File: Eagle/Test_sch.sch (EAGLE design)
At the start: 2 parts, among them U1 APR9600_DIP-28, U2 APR9600_DIP-28

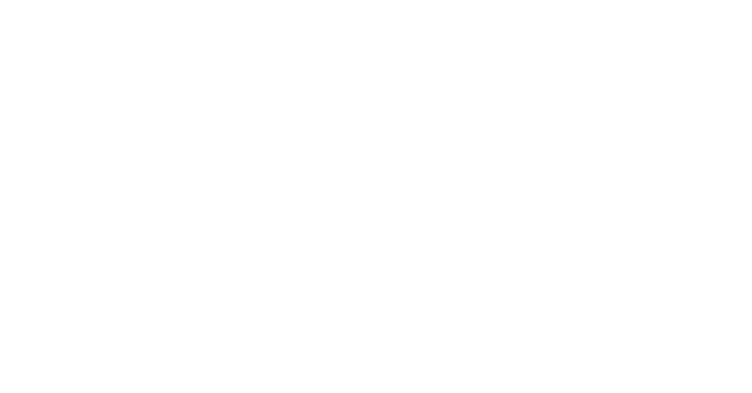
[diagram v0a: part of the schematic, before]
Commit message: La til Buzzer
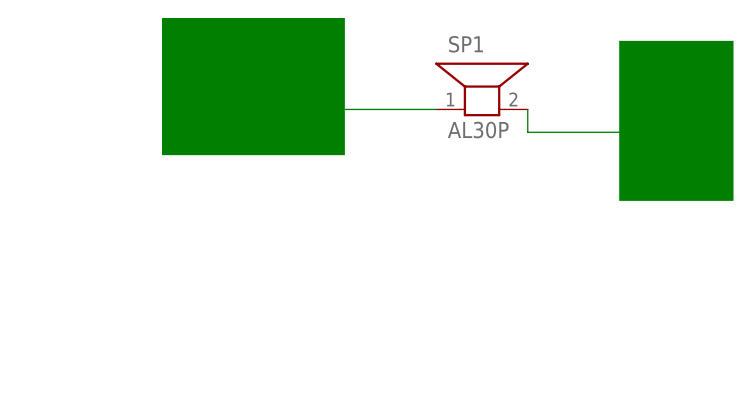
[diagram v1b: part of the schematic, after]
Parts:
- added SP1: AL30P, buzzer:AL30P
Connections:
- new net N$3: SP1.1
- new net N$4: SP1.2
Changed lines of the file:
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@@
 <part name="U1" library="aplus" library_urn="urn:adsk.eagle:library:103" deviceset="APR9600_DIP-28" device="" package3d_urn="urn:adsk.eagle:package:4145/1"/>
 <part name="U2" library="aplus" library_urn="urn:adsk.eagle:library:103" deviceset="APR9600_DIP-28" device="" package3d_urn="urn:adsk.eagle:package:4145/1"/>
+<part name="SP1" library="buzzer" library_urn="urn:adsk.eagle:library:113" deviceset="AL30P" device="" package3d_urn="urn:adsk.eagle:package:5288/1"/>
 </parts>
 <sheets>
 <sheet>
 <plain>
+<rectangle x1="10.16" y1="111.76" x2="30.48" y2="127" layer="91"/>
+<rectangle x1="60.96" y1="106.68" x2="73.66" y2="124.46" layer="91"/>
 </plain>
 <instances>
@@
 <attribute name="NAME" x="-60.8584" y="77.47" size="2.0828" layer="95" ratio="10" rot="SR0"/>
 <attribute name="VALUE" x="-62.5856" y="2.6162" size="2.0828" layer="96" ratio="10" rot="SR0"/>
+</instance>
+<instance part="SP1" gate="G$1" x="45.72" y="116.84" smashed="yes">
+<attribute name="NAME" x="41.91" y="123.19" size="1.778" layer="95"/>
+<attribute name="VALUE" x="41.91" y="113.665" size="1.778" layer="96"/>
 </instance>
 </instances>
@@
 </segment>
 </net>
+<net name="N$3" class="0">
+<segment>
+<pinref part="SP1" gate="G$1" pin="1"/>
+<wire x1="40.64" y1="116.84" x2="30.48" y2="116.84" width="0.1524" layer="91"/>
+</segment>
+</net>
+<net name="N$4" class="0">
+<segment>
+<pinref part="SP1" gate="G$1" pin="2"/>
+<wire x1="50.8" y1="116.84" x2="50.8" y2="114.3" width="0.1524" layer="91"/>
+<wire x1="50.8" y1="114.3" x2="66.04" y2="114.3" width="0.1524" layer="91"/>
+</segment>
+</net>
